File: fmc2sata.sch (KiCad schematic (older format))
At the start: 0 parts

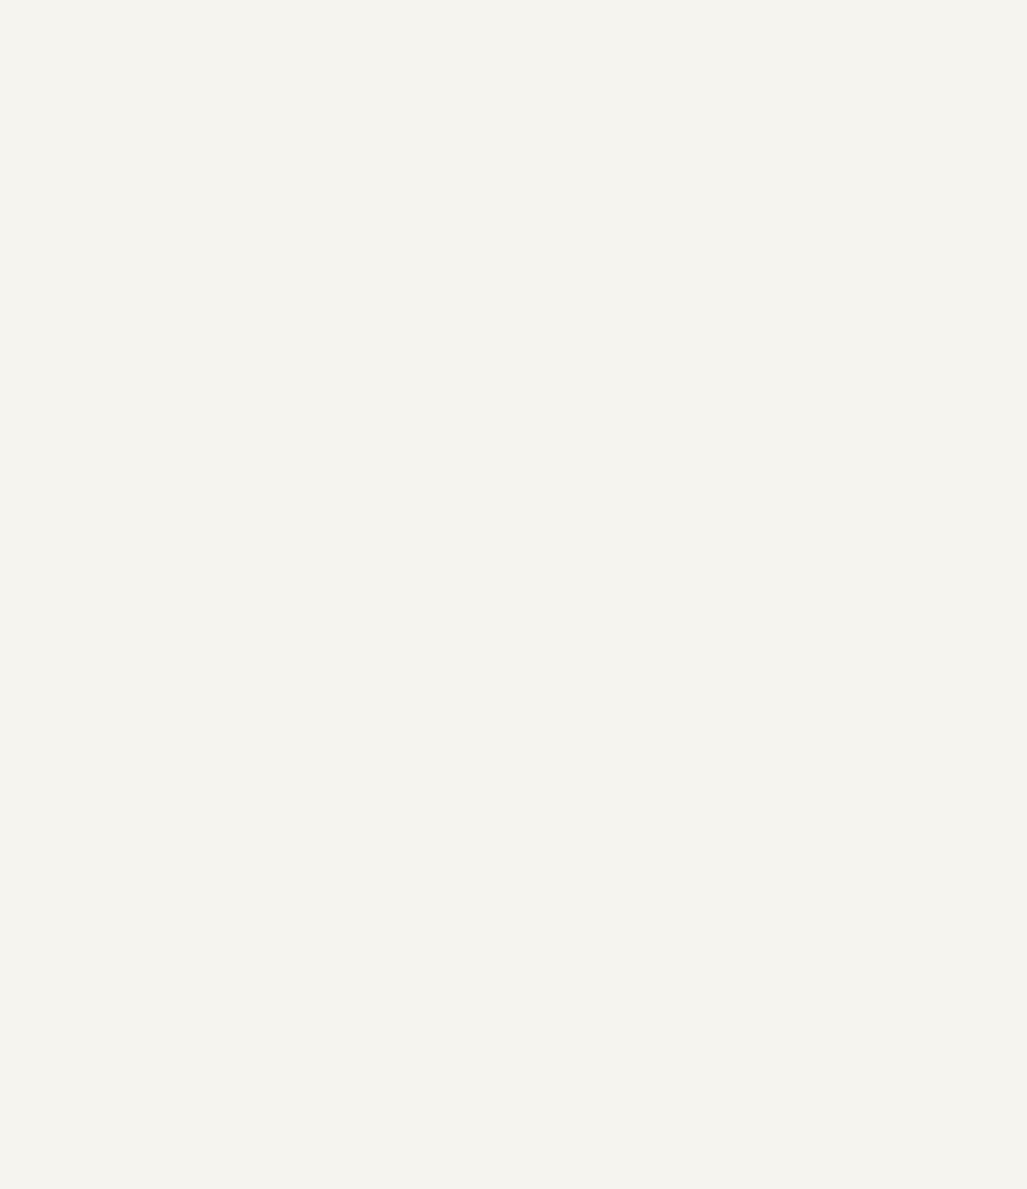
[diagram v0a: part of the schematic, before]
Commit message: Add FMC male connector
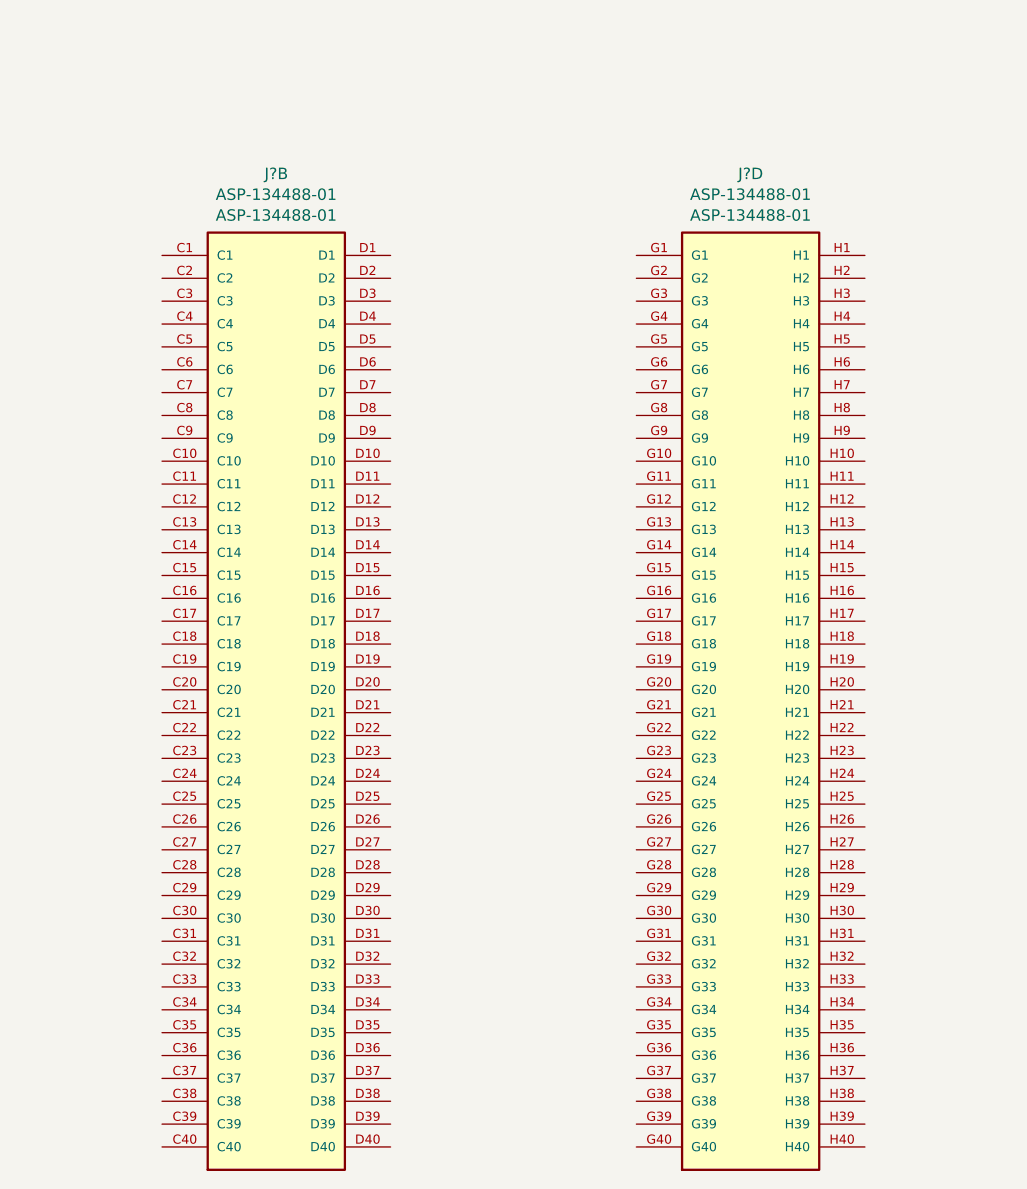
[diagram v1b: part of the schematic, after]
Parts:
- added J? (x2): ASP-134488-01, antmicro-footprints:ASP-134488-01, symbol antmicroFMCConnectors:ASP-134488-01
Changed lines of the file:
@@
 Text Notes 925  1450 0    79   ~ 0
 https://reference.digilentinc.com/reference/programmable-logic/nexys-video/start
+$Comp
+L antmicroFMCConnectors:ASP-134488-01 J?
+U 2 1 6005B4DB
+P 3675 5200
+F 0 "J?" H 3675 7557 50  0000 C CNN
+F 1 "ASP-134488-01" H 3675 7466 50  0000 C CNN
+F 2 "antmicro-footprints:ASP-134488-01" H 3675 5200 50  0001 L BNN
+F 3 "" H 3675 5200 50  0001 L BNN
+F 4 "Samtec" H 3675 5200 50  0001 L BNN "Manufacturer"
+F 5 "ASP-134488-01" H 3675 7375 50  0000 C CNN "MPN"
+	2    3675 5200
+	1    0    0    -1
+$EndComp
+$Comp
+L antmicroFMCConnectors:ASP-134488-01 J?
+U 4 1 6005FF72
+P 5750 5200
+F 0 "J?" H 5750 7557 50  0000 C CNN
+F 1 "ASP-134488-01" H 5750 7466 50  0000 C CNN
+F 2 "antmicro-footprints:ASP-134488-01" H 5750 5200 50  0001 L BNN
+F 3 "" H 5750 5200 50  0001 L BNN
+F 4 "Samtec" H 5750 5200 50  0001 L BNN "Manufacturer"
+F 5 "ASP-134488-01" H 5750 7375 50  0000 C CNN "MPN"
+	4    5750 5200
+	1    0    0    -1
+$EndComp
 $EndSCHEMATC

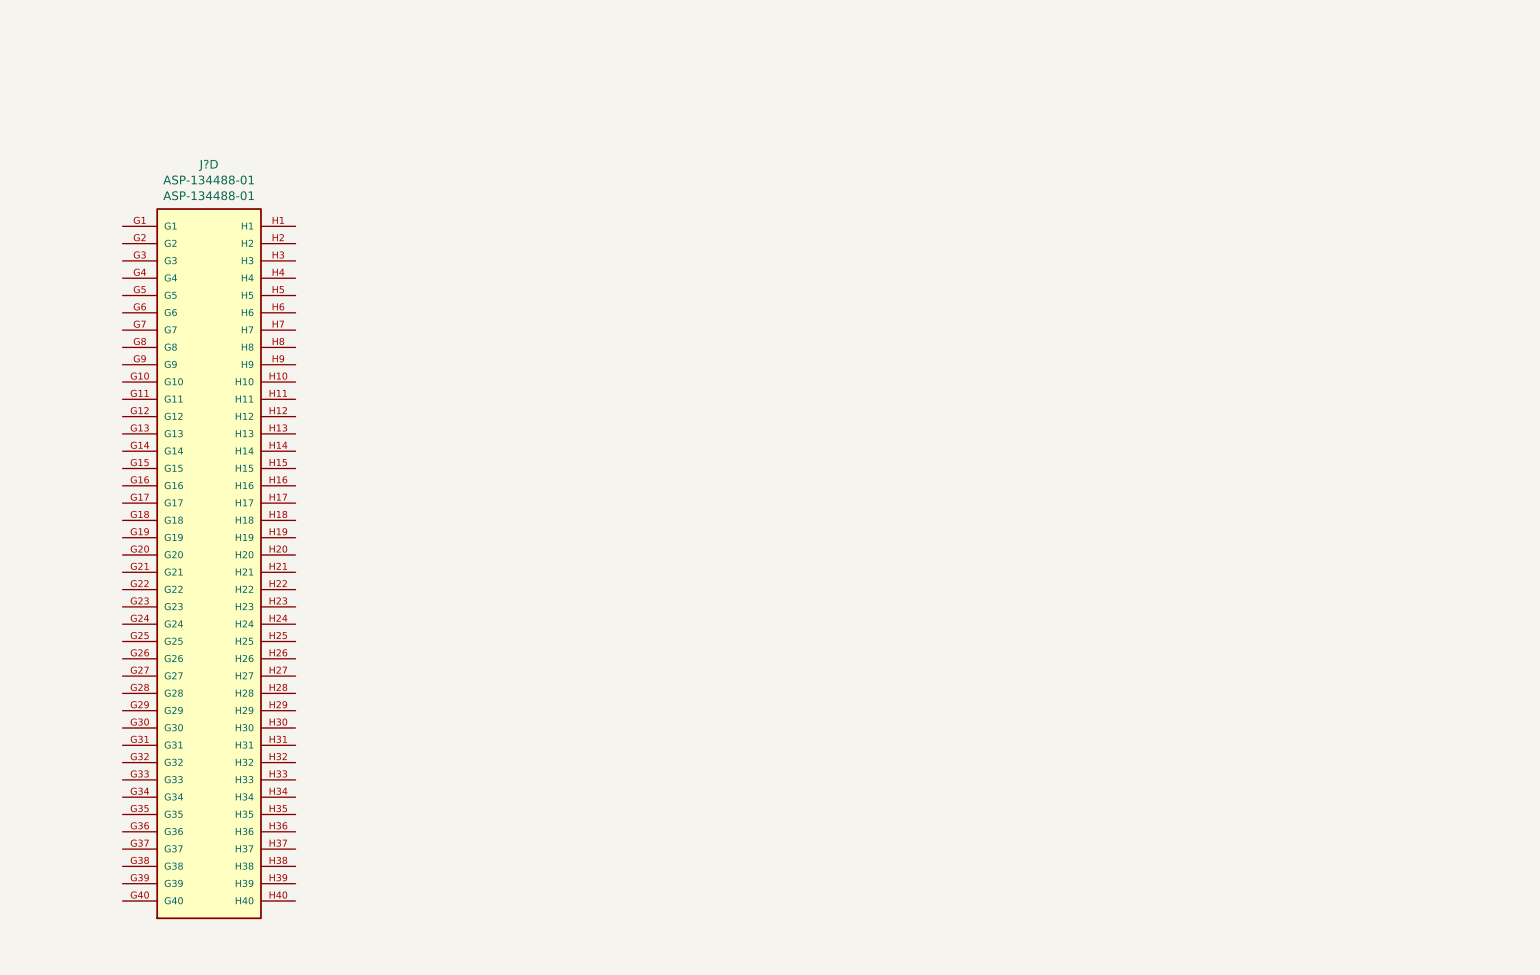
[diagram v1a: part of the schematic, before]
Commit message: Add M.2 with basic connections
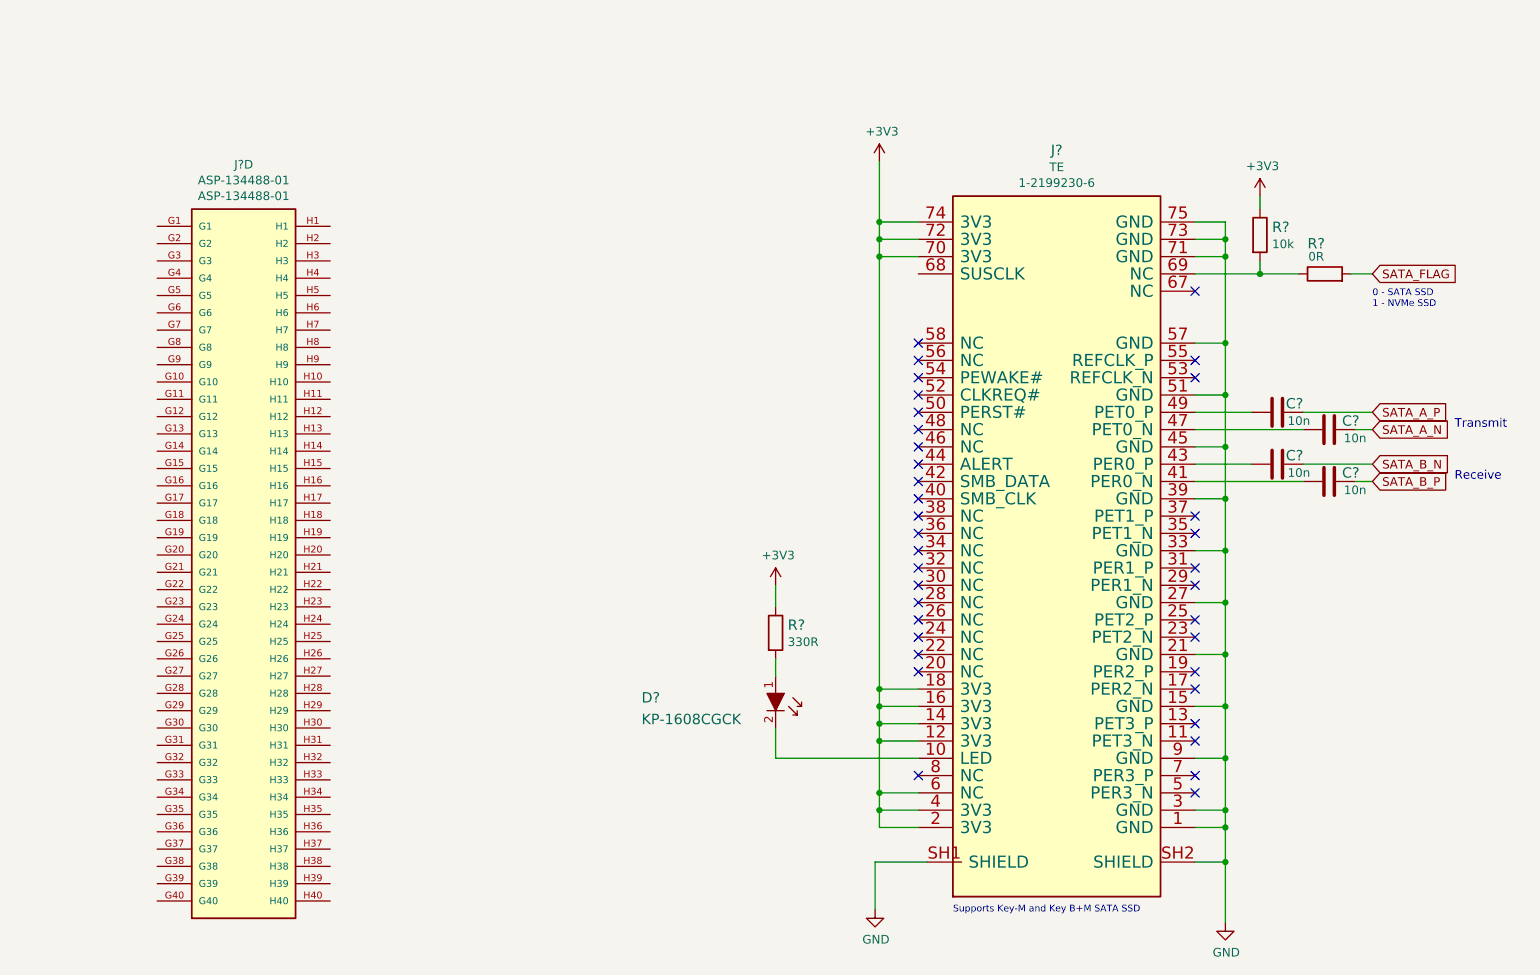
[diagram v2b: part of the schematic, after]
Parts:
- added C? (x4): C_10n_0402, antmicro-footprints:0402-cap, symbol antmicroCapacitors0402:C_10n_0402
- added D?: KP-1608CGCK, antmicro-footprints:LED_0603, symbol antmicroLEDIndicationDiscrete:KP-1608CGCK
- added J?: 1-2199230-6, antmicro-footprints:1-2199230-6, symbol antmicroPciConnectors:1-2199230-6
- added R?: R_330R_0402, antmicro-footprints:0402-res, symbol antmicroResistors0402:R_330R_0402
- added R?: R_10k_0402, antmicro-footprints:0402-res, symbol antmicroResistors0402:R_10k_0402
- added R?: R_0R_0402, antmicro-footprints:0402-res, symbol antmicroResistors0402:R_0R_0402
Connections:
- new net: D?.2, J?.10 (LED)
- new net: C?.2, J?.41 (PER0_N)
- new net: C?.2, J?.43 (PER0_P)
- new net: C?.2, J?.47 (PET0_N)
- new net: C?.2, J?.49 (PET0_P)
- new net: J?.69 (NC), R?.1, R?.2
- new net: D?.1, R?.2
- new net +3V3: J?.12 (3V3), J?.14 (3V3), J?.16 (3V3), J?.18 (3V3), J?.2 (3V3), J?.4 (3V3), J?.6 (NC), J?.70 (3V3), J?.72 (3V3), J?.74 (3V3), R?.1, R?.1
- new net GND: J?.1 (GND), J?.15 (GND), J?.21 (GND), J?.27 (GND), J?.3 (GND), J?.33 (GND), J?.39 (GND), J?.45 (GND), J?.51 (GND), J?.57 (GND), J?.71 (GND), J?.73 (GND), J?.75 (GND), J?.9 (GND), J?.SH1 (SHIELD), J?.SH2 (SHIELD)
- new net SATA_A_N: C?.1
- new net SATA_A_P: C?.1
- new net SATA_B_N: C?.1
- new net SATA_B_P: C?.1
- new net SATA_FLAG: R?.2
- no-connect marks 0 -> 36
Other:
- note added: "0 - SATA SSD\n1 - NVMe SSD"
- note added: "Receive"
- note added: "Supports Key-M and Key B+M SATA SSD"
- note added: "Transmit"
- moved on the sheet: J?D
